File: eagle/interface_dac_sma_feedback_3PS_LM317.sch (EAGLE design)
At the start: 38 parts, among them IC1 ISO1540, X1 BU-SMA-V

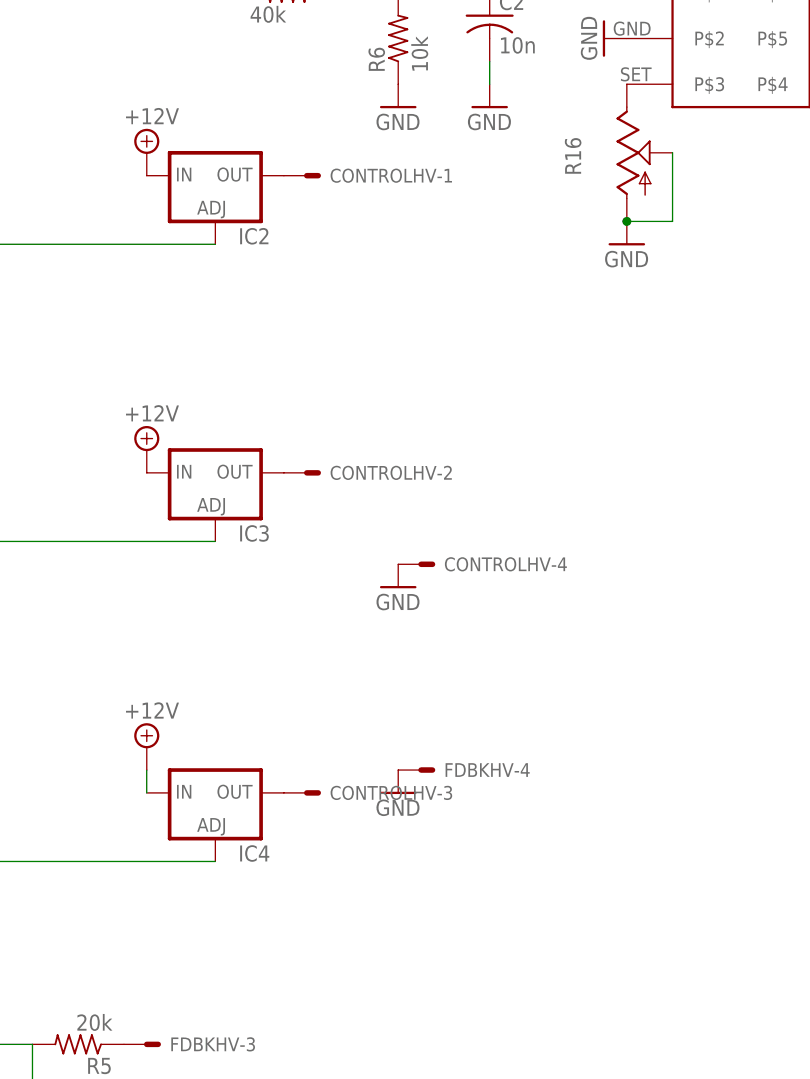
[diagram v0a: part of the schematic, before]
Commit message: ultra layout. try that next time with lm317 interface
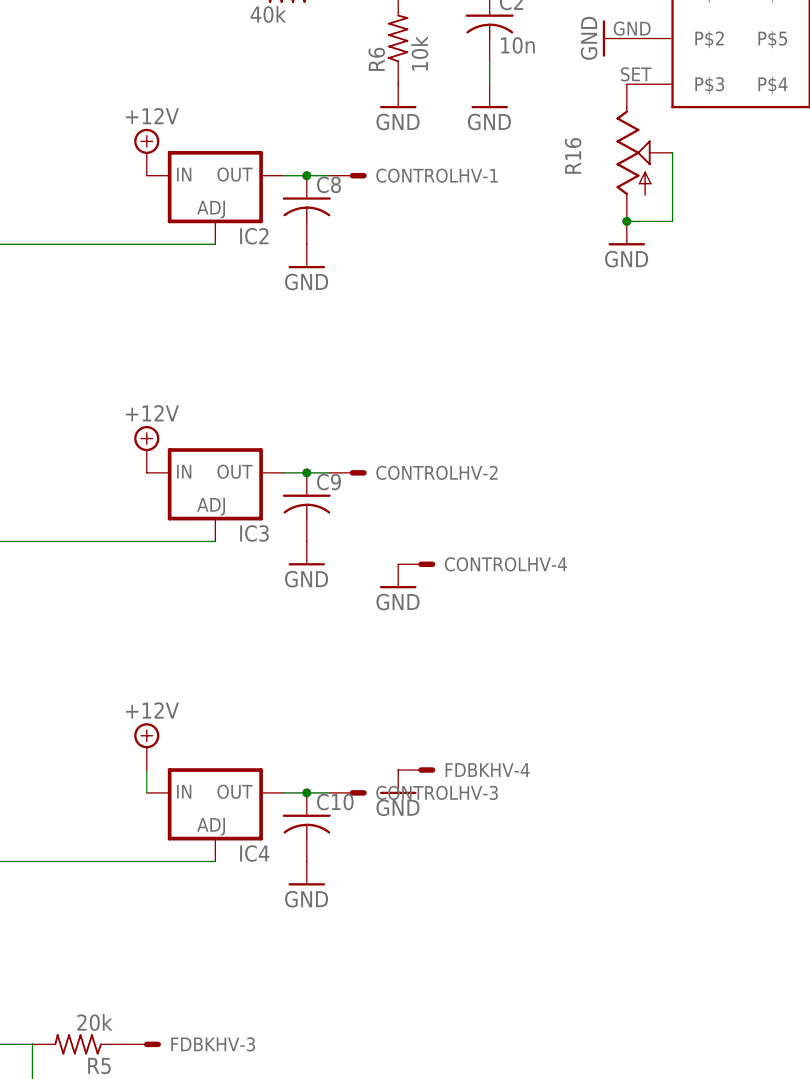
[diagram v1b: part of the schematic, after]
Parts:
- added C10, C8, C9: (no value), resistor:C-US075-063X106
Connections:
- net GND: now also C10.2, C8.2, C9.2
- net N$11: now also C9.1
- net N$4: now also C8.1
- net N$5: now also C10.1
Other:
- moved on the sheet: CONTROLHV-1, CONTROLHV-2, CONTROLHV-3
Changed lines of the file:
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@@
 <part name="R11" library="resistor" deviceset="R-US_" device="0207/12" value="20k"/>
 <part name="R12" library="resistor" deviceset="R-US_" device="0207/12" value="12"/>
+<part name="C8" library="resistor" deviceset="C-US" device="075-063X106"/>
+<part name="C9" library="resistor" deviceset="C-US" device="075-063X106"/>
+<part name="C10" library="resistor" deviceset="C-US" device="075-063X106"/>
+<part name="GND21" library="supply1" deviceset="GND" device=""/>
+<part name="GND24" library="supply1" deviceset="GND" device=""/>
+<part name="GND25" library="supply1" deviceset="GND" device=""/>
 </parts>
 <sheets>
@@
 <instance part="GND12" gate="1" x="167.64" y="48.26"/>
 <instance part="P+8" gate="+12V" x="200.66" y="68.58"/>
-<instance part="CONTROLHV" gate="-1" x="218.44" y="99.06"/>
-<instance part="CONTROLHV" gate="-2" x="218.44" y="66.04"/>
-<instance part="CONTROLHV" gate="-3" x="218.44" y="30.48"/>
+<instance part="CONTROLHV" gate="-1" x="223.52" y="99.06"/>
+<instance part="CONTROLHV" gate="-2" x="223.52" y="66.04"/>
+<instance part="CONTROLHV" gate="-3" x="223.52" y="30.48"/>
 <instance part="CONTROLHV" gate="-4" x="231.14" y="55.88"/>
 <instance part="FDBKHV" gate="-1" x="162.56" y="73.66"/>
@@
 <instance part="R11" gate="G$1" x="147.32" y="83.82"/>
 <instance part="R12" gate="G$1" x="144.78" y="73.66"/>
+<instance part="C8" gate="G$1" x="218.44" y="96.52"/>
+<instance part="C9" gate="G$1" x="218.44" y="63.5"/>
+<instance part="C10" gate="G$1" x="218.44" y="27.94"/>
+<instance part="GND21" gate="1" x="218.44" y="88.9"/>
+<instance part="GND24" gate="1" x="218.44" y="55.88"/>
+<instance part="GND25" gate="1" x="218.44" y="20.32"/>
 </instances>
 <busses>
@@
 <pinref part="C7" gate="G$1" pin="2"/>
 <pinref part="GND20" gate="1" pin="GND"/>
+</segment>
+<segment>
+<pinref part="C8" gate="G$1" pin="2"/>
+<pinref part="GND21" gate="1" pin="GND"/>
+</segment>
+<segment>
+<pinref part="C9" gate="G$1" pin="2"/>
+<pinref part="GND24" gate="1" pin="GND"/>
+</segment>
+<segment>
+<pinref part="C10" gate="G$1" pin="2"/>
+<pinref part="GND25" gate="1" pin="GND"/>
 </segment>
 </net>
@@
 <pinref part="CONTROLHV" gate="-1" pin="S"/>
 <pinref part="IC2" gate="1" pin="OUT"/>
+<wire x1="220.98" y1="99.06" x2="218.44" y2="99.06" width="0.1524" layer="91"/>
+<pinref part="C8" gate="G$1" pin="1"/>
+<wire x1="218.44" y1="99.06" x2="215.9" y2="99.06" width="0.1524" layer="91"/>
+<junction x="218.44" y="99.06"/>
 </segment>
 </net>
@@
 <pinref part="CONTROLHV" gate="-3" pin="S"/>
 <pinref part="IC4" gate="1" pin="OUT"/>
+<wire x1="220.98" y1="30.48" x2="218.44" y2="30.48" width="0.1524" layer="91"/>
+<pinref part="C10" gate="G$1" pin="1"/>
+<wire x1="218.44" y1="30.48" x2="215.9" y2="30.48" width="0.1524" layer="91"/>
+<junction x="218.44" y="30.48"/>
 </segment>
 </net>
@@
 <pinref part="CONTROLHV" gate="-2" pin="S"/>
 <pinref part="IC3" gate="1" pin="OUT"/>
-</segment>
-</net>
+<wire x1="220.98" y1="66.04" x2="218.44" y2="66.04" width="0.1524" layer="91"/>
+<pinref part="C9" gate="G$1" pin="1"/>
+<wire x1="218.44" y1="66.04" x2="215.9" y2="66.04" width="0.1524" layer="91"/>
+<junction x="218.44" y="66.04"/>
+</segment>
+</net>

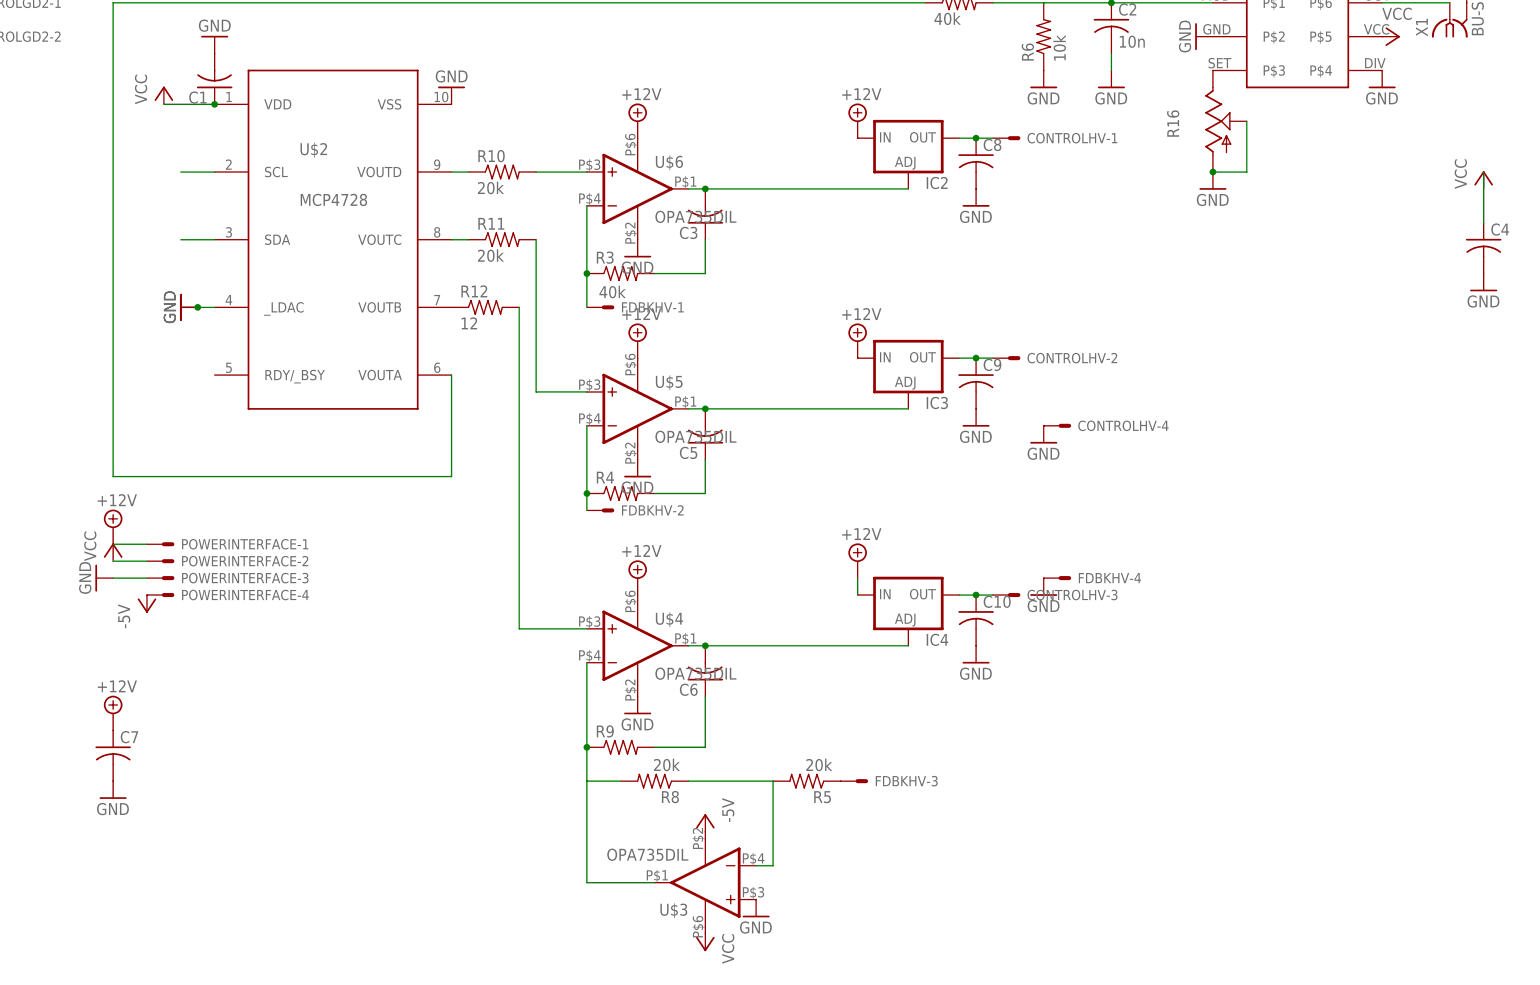
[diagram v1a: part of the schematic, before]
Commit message: Fix negative rail problems
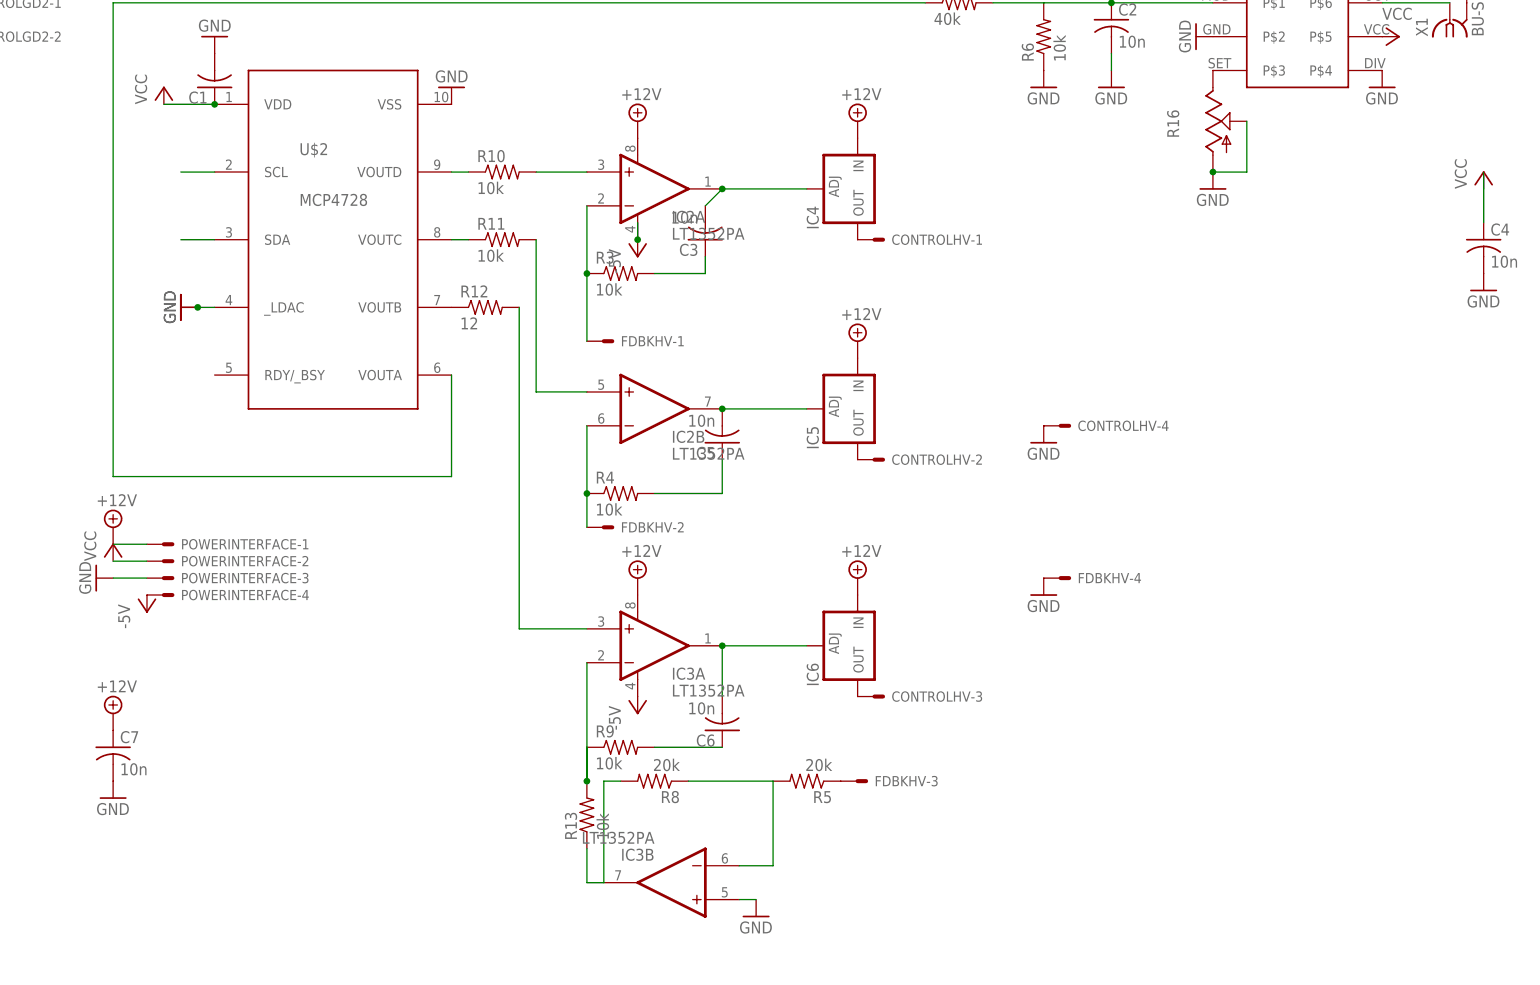
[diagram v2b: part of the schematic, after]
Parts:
- removed C10, C8, C9: (no value), resistor:C-US075-063X106
- removed U$3, U$4, U$5, U$6: OPA735DIL, texas:OPA735DIL
- added IC5, IC6: (no value), v-reg:LM317TS
- added R13: 10k, resistor:R-US_0207/12
- C3, C4, C5, C6, C7: value (none) -> 10n
- FDBKHV: value 40k -> (none)
- IC2, IC3: value (none) -> LT1352PA; device v-reg:LM317TS -> linear-technology:LT1352PA
- R10, R11: value 20k -> 10k
- R3, R4, R9: value (none) -> 10k
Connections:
- new net N$27: IC3A.-IN, R13.2, R9.1
- net +12V: now also IC2A.V+, IC3A.V+, IC5.IN, IC6.IN; no longer IC2.IN, IC3.IN, U$4.V+, U$5.V+, U$6.V+
- net -5V: now also IC2A.V-, IC3A.V-; no longer U$3.V-
- net GND: now also IC3B.+IN; no longer C10.2, C8.2, C9.2, U$3.+IN, U$4.V-, U$5.V-, U$6.V-
- net N$10: now also IC2B.OUT, IC5.ADJ; no longer IC3.ADJ, U$5.OUT
- net N$11: now also CONTROLHV-3.S, IC6.OUT; no longer C9.1, CONTROLHV-2.S, IC3.OUT
- net N$14: now also IC3B.OUT, R13.1; no longer R9.1, U$3.OUT, U$4.-IN
- net N$16: now also IC2A.+IN; no longer U$6.+IN
- net N$17: now also IC2B.+IN; no longer U$5.+IN
- net N$18: now also IC3A.+IN; no longer U$4.+IN
- net N$19: now also IC2A.OUT, IC4.ADJ; no longer IC2.ADJ, U$6.OUT
- net N$21: now also IC3A.OUT, IC6.ADJ; no longer IC4.ADJ, U$4.OUT
- net N$23: now also IC3B.-IN; no longer U$3.-IN
- net N$4: now also IC4.OUT; no longer C8.1, IC2.OUT
- net N$5: now also CONTROLHV-2.S, IC5.OUT; no longer C10.1, CONTROLHV-3.S, IC4.OUT
- net N$6: now also IC2B.-IN; no longer U$5.-IN
- net N$8: now also IC2A.-IN; no longer U$6.-IN
- net VCC: no longer U$3.V+
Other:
- moved on the sheet: C3, C5, C6, CONTROLHV-1, CONTROLHV-2, CONTROLHV-3, FDBKHV-1, FDBKHV-2, IC4

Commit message: optional 317 regulation of emcos
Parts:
- added HVRDOUT+, HVRDOUT-, HVRDOUTCT: (no value), con-molex:KK-156-3
- added Q1, Q2, Q3: TIP122V, transistor-npn:TIP122V
- IC4, IC5, IC6: value (none) -> LM317MABDT; device v-reg:LM317TS -> v-reg:LM317MABDT
- R12: value 12 -> 10k
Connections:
- net +12V: now also HVRDOUT+-1.S, HVRDOUT--1.S, HVRDOUTCT-1.S, Q1.C, Q2.C, Q3.C
- net GND: now also HVRDOUT+-3.S, HVRDOUT--3.S, HVRDOUTCT-3.S
- net N$10: now also Q2.B
- net N$11: now also CONTROLHV-2.S, IC5.OUT, Q2.E; no longer CONTROLHV-3.S, IC6.OUT
- net N$14: now also HVRDOUT--2.S
- net N$19: now also Q1.B
- net N$21: now also Q3.B
- net N$4: now also Q1.E
- net N$5: now also CONTROLHV-3.S, IC6.OUT, Q3.E; no longer CONTROLHV-2.S, IC5.OUT
- net N$6: now also HVRDOUTCT-2.S
- net N$8: now also HVRDOUT+-2.S
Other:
- note added: "Allows either LM317 or 2N6387 NOT BOTH"
- moved on the sheet: C1, C2, C3, C4, C5, C6, C7, CONTROLGD2-1, CONTROLGD2-2, CONTROLHV-1, CONTROLHV-2, CONTROLHV-3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
